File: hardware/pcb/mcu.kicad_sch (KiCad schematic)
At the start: 15 parts, among them J1 Conn_02x03_Odd_Even, U6 ESP32-S3-WROOM-1, U8 NRF24L01_Breakout

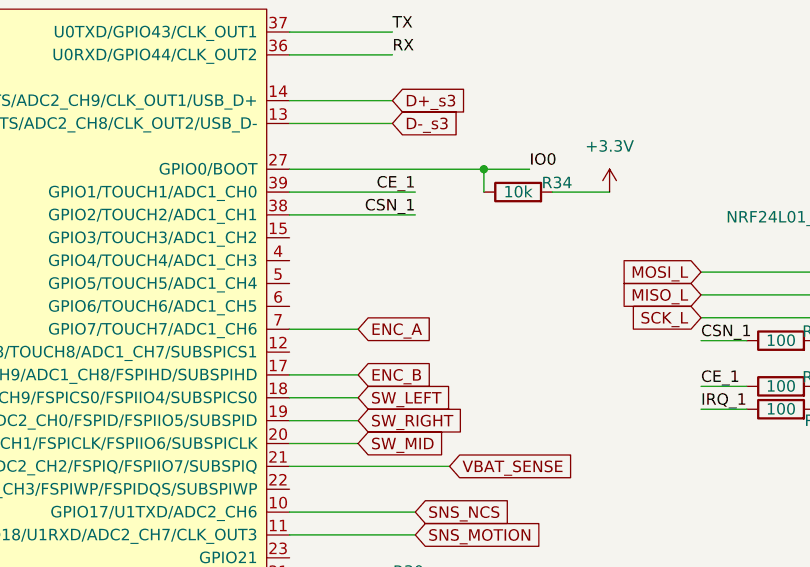
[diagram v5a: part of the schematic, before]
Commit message: contacts NC des trois clics : anti-rebond par SPDT
Les switches de la coque M100 sont des SPDT. Le schema n'exploitait que COM et
NO, les pins NC portaient un no_connect et leurs pads restaient en l'air.

On lit maintenant les DEUX contacts. Au repos NC est ferme sur COM donc bas et
NO ouvert donc haut ; au clic ils s'inversent. Pendant le rebond les deux sont
hauts : le firmware garde alors l'etat precedent, ce qui supprime le double-clic
sans aucun filtrage temporel.

  SW_LEFT_NC  -> GPIO4    SW_RIGHT_NC -> GPIO5    SW_MID_NC -> GPIO6
  pull-ups 10 k R108/R109/R110, en miroir des R105-R107 des NO

L'ERC y GAGNE 3 erreurs (14 -> 11) : GPIO4/5/6 etaient des pins libres
signalees pin_not_connected. Netlist verifiee, chaque net NC a exactement
3 noeuds. DRC 26/20 inchange, 0 pad non connecte. Placement et routage par Mae.

CORRECTION DE DOCUMENTATION : le README donnait "SW_LEFT 18, SW_RIGHT 19,
SW_MID 20" — ce sont les NUMEROS DE BROCHE du module, pas les GPIO, qui valent
10/11/12. Idem SNS_NCS (GPIO17, broche 10) et SNS_MOTION (GPIO18, broche 11).
Verifie en recoupant lib_symbols, les fils et la netlist. Le tableau donne
desormais les deux colonnes. Le module au BOM est un N8R2 (C2913204), pas le
N16R8 dont parlait le README — la mention de PSRAM octale est retiree.

Co-Authored-By: Claude Opus 5 <noreply@anthropic.com>
Claude-Session: https://claude.ai/code/session_01GfX5RmekmQi78Dm37qsT4Z
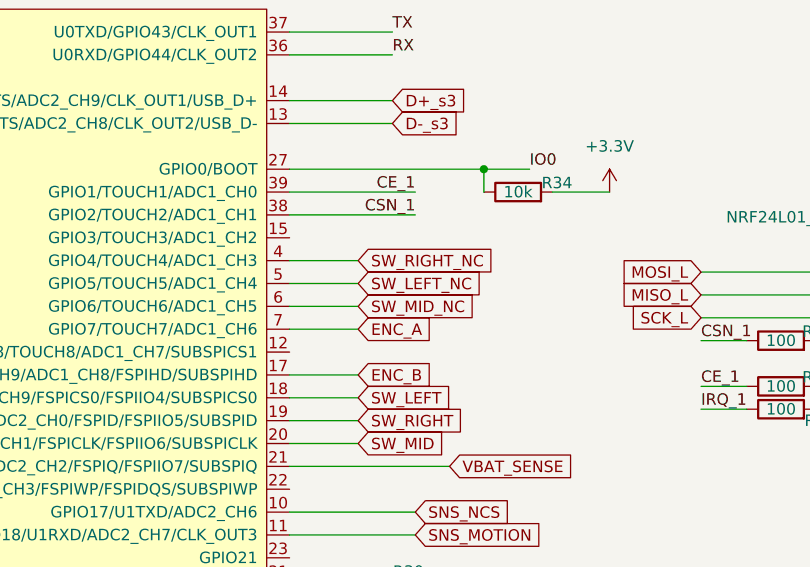
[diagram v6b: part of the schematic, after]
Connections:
- net SW_RIGHT_NC: now reaches U6.4 (GPIO4/TOUCH4/ADC1_CH3)
- net SW_LEFT_NC: now reaches U6.5 (GPIO5/TOUCH5/ADC1_CH4)
- net SW_MID_NC: now reaches U6.6 (GPIO6/TOUCH6/ADC1_CH5)
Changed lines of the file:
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@@
+	(wire
+		(pts
+			(xy 172.72 60.96) (xy 180.34 60.96)
+		)
+		(stroke
+			(width 0)
+			(type default)
+		)
+	)
 	(wire
 		(pts
@@
 	(wire
 		(pts
+			(xy 172.72 63.5) (xy 180.34 63.5)
+		)
+		(stroke
+			(width 0)
+			(type default)
+		)
+	)
+	(wire
+		(pts
 			(xy 55.88 53.34) (xy 81.28 53.34)
 		)
@@
 		(pts
 			(xy 218.44 72.39) (xy 223.52 72.39)
+		)
+		(stroke
+			(width 0)
+			(type default)
+		)
+	)
+	(wire
+		(pts
+			(xy 172.72 58.42) (xy 180.34 58.42)
 		)
 		(stroke
@@
 		)
 	)
+	(global_label "SW_RIGHT_NC"
+		(shape input)
+		(at 180.34 58.42 0)
+		(fields_autoplaced yes)
+		(effects
+			(font
+				(size 1.27 1.27)
+			)
+			(justify left)
+		)
+		(property "Intersheetrefs" "${INTERSHEET_REFS}"
+			(at 180.34 58.42 0)
+			(hide yes)
+			(show_name no)
+			(do_not_autoplace no)
+			(effects
+				(font
+					(size 1.27 1.27)
+				)
+			)
+		)
+	)
 	(global_label "SCK_L"
 		(shape input)
@@
 		)
 	)
+	(global_label "SW_LEFT_NC"
+		(shape input)
+		(at 180.34 60.96 0)
+		(fields_autoplaced yes)
+		(effects
+			(font
+				(size 1.27 1.27)
+			)
+			(justify left)
+		)
+		(property "Intersheetrefs" "${INTERSHEET_REFS}"
+			(at 180.34 60.96 0)
+			(hide yes)
+			(show_name no)
+			(do_not_autoplace no)
+			(effects
+				(font
+					(size 1.27 1.27)
+				)
+			)
+		)
+	)
 	(global_label "VBAT_SENSE"
 		(shape input)
@@
 			)
 		)
+	)
+	(global_label "SW_MID_NC"
+		(shape input)
+		(at 180.34 63.5 0)
+		(fields_autoplaced yes)
+		(effects
+			(font
+				(size 1.27 1.27)
+			)
+			(justify left)
+		)
+		(property "Intersheetrefs" "${INTERSHEET_REFS}"
+			(at 180.34 63.5 0)
+			(hide yes)
+			(show_name no)
+			(do_not_autoplace no)
+			(effects
+				(font
+					(size 1.27 1.27)
+				)
+			)
+		)

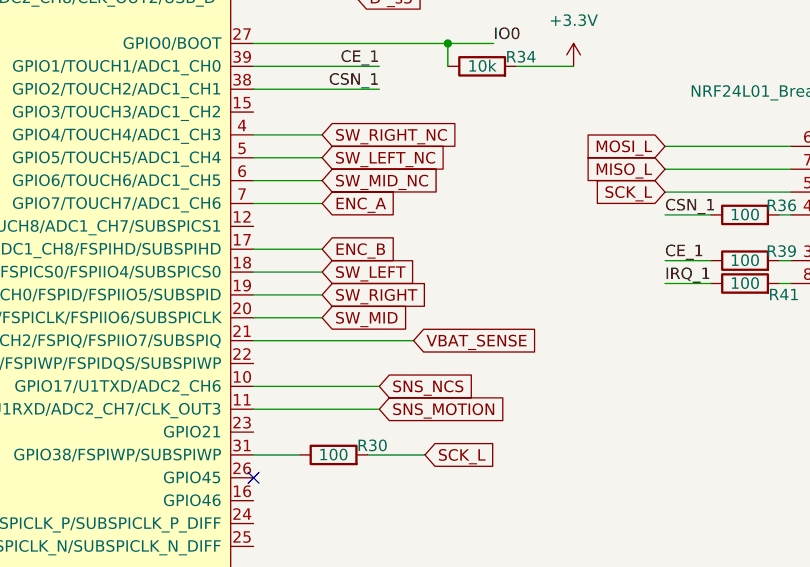
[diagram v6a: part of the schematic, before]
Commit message: schema REV2 : LQ1 recable, D100 supprimee, VBAT_SENSE sur ADC1, U100 corrige
LQ1 etait cable a l'envers depuis le portage du fork USB-Mouse. Le symbole
Optical_Mouse:LQ ne nommait ses broches que "1, 2, 3", sans fonction, et le
portage a suppose un double phototransistor A/COM/B. Le schema d'origine de la
M100 dit autre chose : broche 1 = DATA, 2 = VCC, 3 = GND.

La carte alimentait donc le capteur a l'envers — son VCC a la masse, sa masse
tiree au 3,3 V par R104. Le courant passait par la diode de substrat interne et
clampait les deux nets a 0,65 V, insensible a la lumiere comme au pilotage.
Deux LQ1 ont ete dessoudes avant que la confrontation au schema source ne donne
la reponse.

  - LQ1.2 -> +3V3, LQ1.3 -> GND, LQ1.1 (DATA) reste sur ENC_A / GPIO7
  - LD1 cathode -> R102 -> GPIO9, renomme ENC_LED : la LED de molette devient
    pilotable, comme sur la M100 d'origine. Gain d'autonomie, et un diagnostic
    qui aurait pris une minute au lieu d'une journee.
  - R102 = 820 ohms : 2,6 mA, le point de fonctionnement d'origine transpose
    du 5 V USB au 3,3 V
  - R104 = 0 ohm (pont vers la masse), R103 conservee
  - symbole LQ : broches nommees DATA / VCC / GND, dans le cache et dans
    optical_mouse.lib, pour que l'erreur soit impossible a refaire

D100 supprimee : le PMW3389 embarque sa LED IR (broche 15 LED_P = anode). La
LED externe etait de surcroit montee a l'envers et bloquait le courant, rendant
le capteur aveugle. R101 = 16 ohms alimentee depuis le rail capteur, renomme
+1V8 -> +2V0.

VBAT_SENSE passe de U6.21 (GPIO13, ADC2_CH2) a U6.12 (GPIO8, ADC1_CH7) :
l'ADC2 de l'ESP32-S3 est partage avec le driver WiFi.

U100 : les numeros de pad du symbole sont corriges — VI porte le pad 3 et VO le
pad 2, soit le brochage reel du XC6206 en SOT-23. Le schema cesse de mentir et
la netlist devient juste d'elle-meme.

Co-Authored-By: Claude Opus 5 (1M context) <noreply@anthropic.com>
Claude-Session: https://claude.ai/code/session_01VhxWZJVUd4SHAcp3eUFVJV
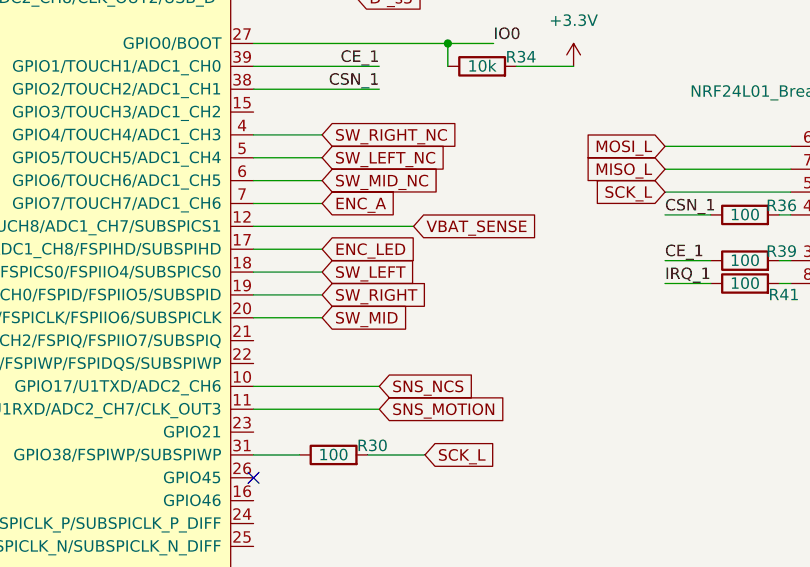
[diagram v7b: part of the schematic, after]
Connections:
- net VBAT_SENSE: now also U6.12 (GPIO8/TOUCH8/ADC1_CH7/SUBSPICS1); no longer U6.21 (GPIO13/TOUCH13/ADC2_CH2/FSPIQ/FSPIIO7/SUBSPIQ)
- net ENC_B renamed ENC_LED
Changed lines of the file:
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@@
 	(wire
 		(pts
-			(xy 190.5 81.28) (xy 172.72 81.28)
+			(xy 190.5 68.58) (xy 172.72 68.58)
 		)
 		(stroke
@@
 	(global_label "VBAT_SENSE"
 		(shape input)
-		(at 190.5 81.28 0)
+		(at 190.5 68.58 0)
 		(fields_autoplaced yes)
 		(effects
@@
 		)
 	)
-	(global_label "ENC_B"
+	(global_label "ENC_LED"
 		(shape input)
 		(at 180.34 71.12 0)
